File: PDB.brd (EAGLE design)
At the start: 143.5 x 151.3 mm, 71 parts

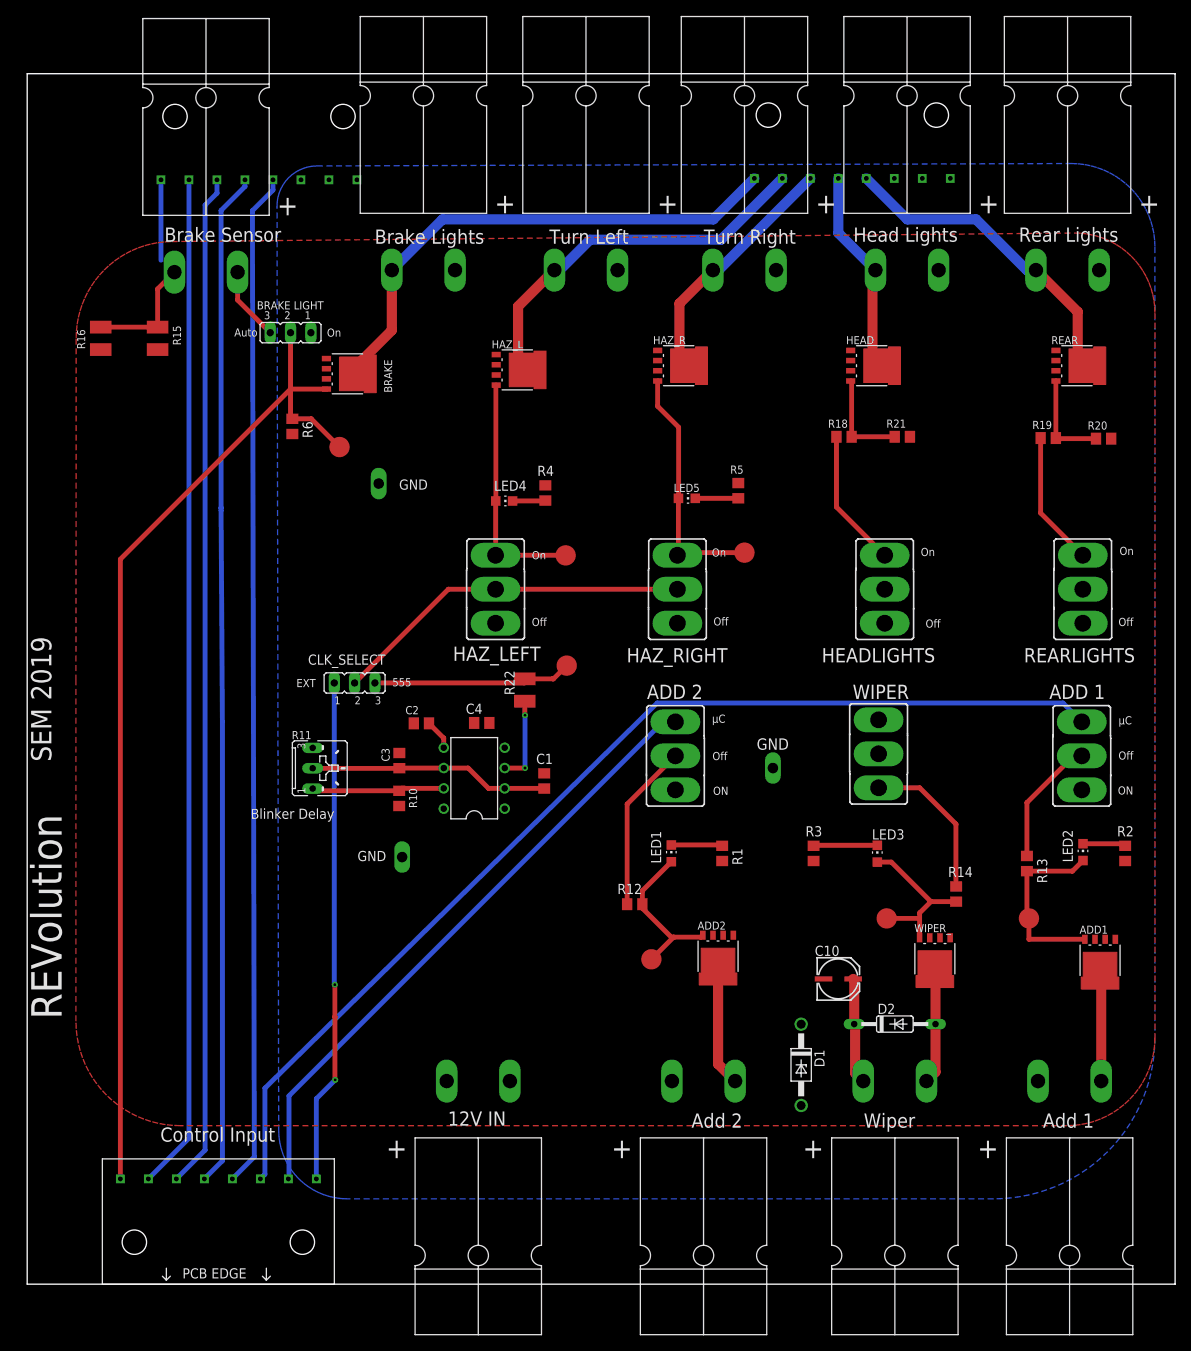
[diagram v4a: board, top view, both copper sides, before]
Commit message: added REV Logo, fixed some hidden airwires
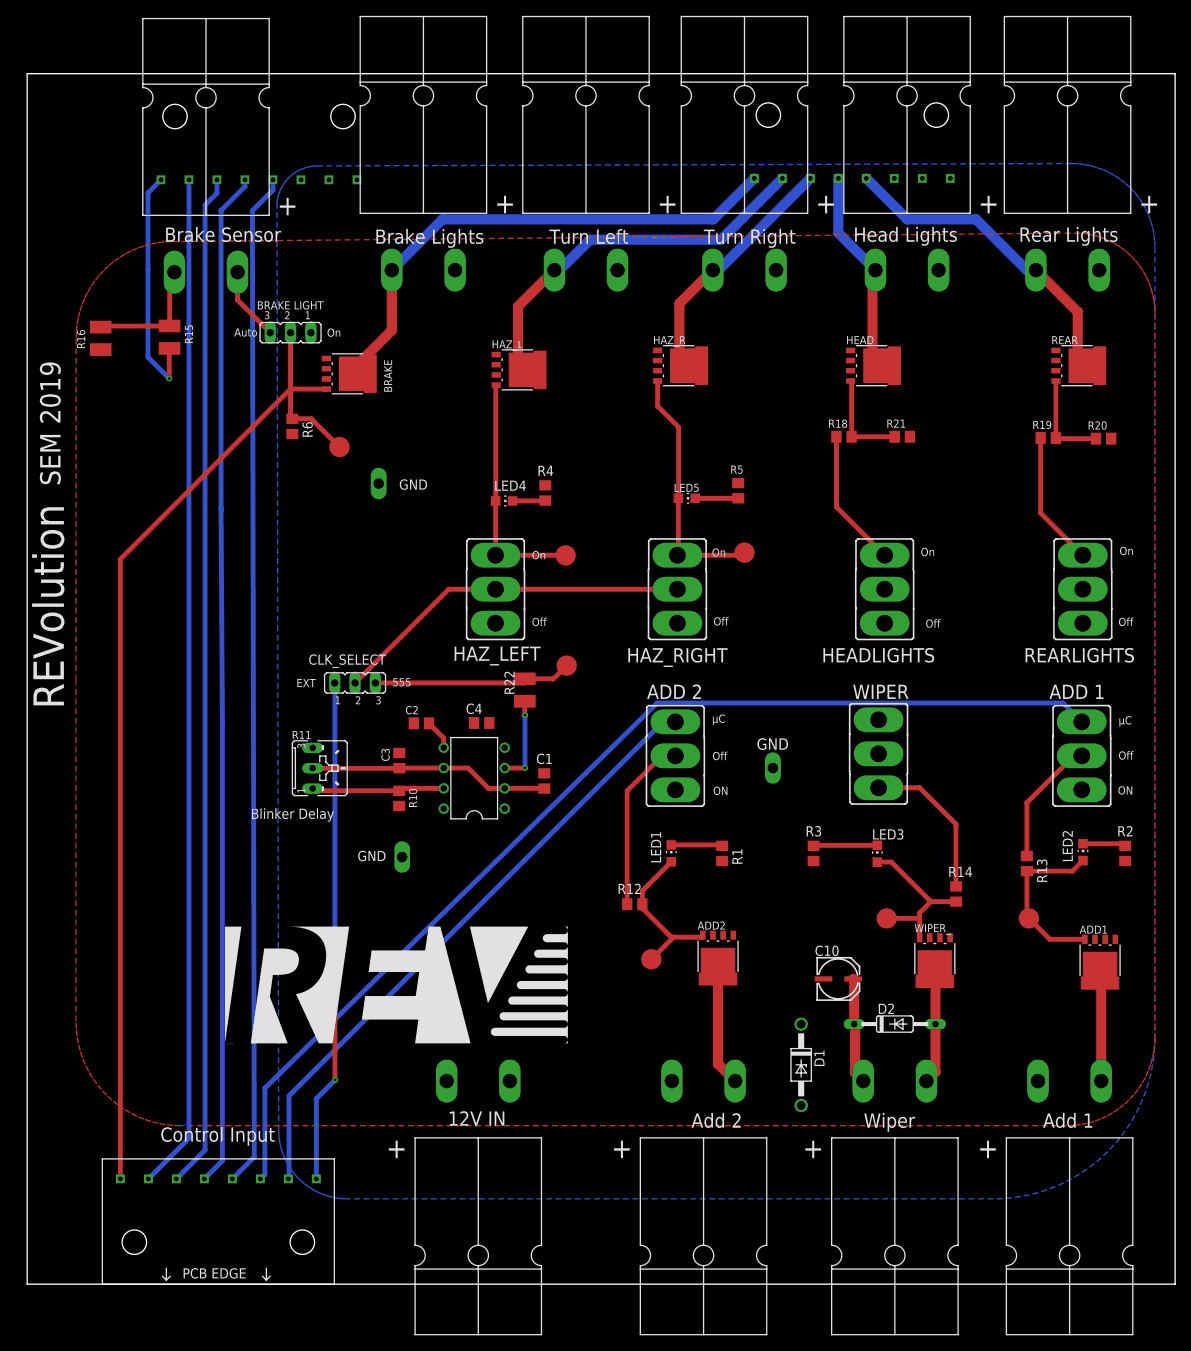
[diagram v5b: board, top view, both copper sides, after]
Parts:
- moved R15 1.51 mm to (26.2, 95.0)
- moved CLK_SELECT 0.06 mm to (49.4, 51.8)
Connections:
- new net BRAKE_SNS_OUT: BRAKE.4, BRAKE_SENSOR_OVERRIDE.2, CONTROL_IN.P1, R6.1, TP7.TP
- net BRAKE_SNS_IN: no longer BRAKE.4, BRAKE_SENSOR_OVERRIDE.2, CONTROL_IN.P1, R6.1, TP7.TP
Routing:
- net BRAKE_SNS_OUT: track 0.00 -> 130.2 mm
- net BRAKE_SNS_IN: track 139.5 -> 9.25 mm
- net VDD: track 23.4 -> 43.7 mm, vias 0 -> 1
- net N$26: track 23.2 -> 21.6 mm
- net H6: track 21.0 -> 22.0 mm
- net SNS_VOLTAGE: track 14.9 -> 15.7 mm
- net H2: track 30.8 -> 31.4 mm
- net H5: track 16.5 -> 15.9 mm
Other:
- board text added: "/Users/louissmidt/Downloads/Untitled-2.BMP"
- board text added: "SPI OUT"
- board text removed: "SPI PT OUT"

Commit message: fixes vdd plane, fixes issues discussed in meeting
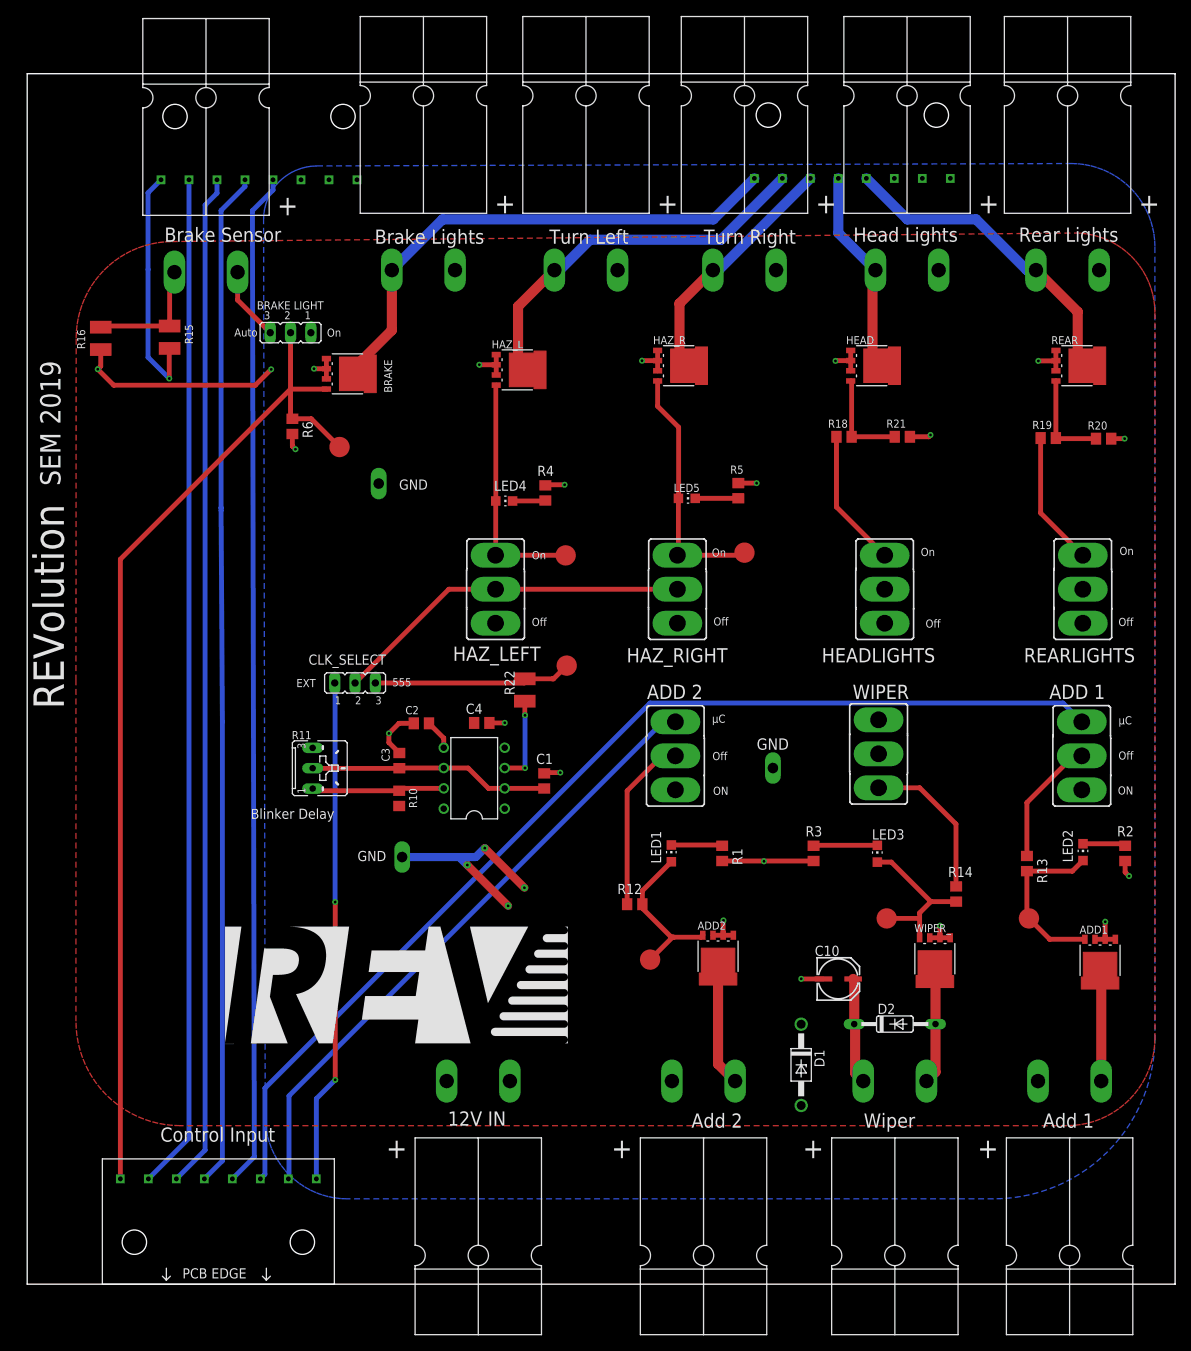
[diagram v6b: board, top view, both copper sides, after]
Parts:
- moved TP2 0.16 mm to (86.2, 17.2)
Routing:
- net GND: track 0.00 -> 126.1 mm, vias 0 -> 25
- net N$7: track 21.1 -> 20.4 mm
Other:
- board text added: "Standoffs"

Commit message: added values
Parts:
- D1: value (none) -> 12V
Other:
- board text removed: "Standoffs"
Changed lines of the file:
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@@
 <layer number="43" name="vRestrict" color="2" fill="10" visible="no" active="yes"/>
 <layer number="44" name="Drills" color="7" fill="1" visible="no" active="yes"/>
-<layer number="45" name="Holes" color="7" fill="1" visible="no" active="yes"/>
+<layer number="45" name="Holes" color="7" fill="1" visible="yes" active="yes"/>
 <layer number="46" name="Milling" color="3" fill="1" visible="no" active="yes"/>
 <layer number="47" name="Measures" color="7" fill="1" visible="no" active="yes"/>
@@
 <text x="36.322" y="34.798" size="1.27" layer="25">Blinker Delay</text>
 <text x="12.547" y="76.421" size="2.54" layer="25" font="vector" ratio="13" rot="R90">SEM 2019</text>
-<text x="12.97" y="48.522" size="3.81" layer="25" rot="R90">REVolution</text>
+<text x="12.97" y="29.222" size="3.81" layer="25" rot="R90">REVolution</text>
 <text x="92.964" y="106.68" size="1.778" layer="25">Turn Right</text>
 <text x="73.66" y="106.68" size="1.778" layer="25">Turn Left</text>
@@
 <rectangle x1="75.59" y1="21.31" x2="75.97" y2="21.33" layer="25"/>
 <text x="33.12" y="6.64" size="0.04" layer="25" font="vector">/Users/louissmidt/Downloads/Untitled-2.BMP</text>
-<text x="9.36" y="120.5" size="1.778" layer="26">Standoffs</text>
+<hole x="14.68" y="122.6" drill="2"/>
+<hole x="12.84" y="-18.42" drill="2"/>
+<hole x="149.16" y="121.88" drill="2"/>
+<hole x="148.68" y="-17.46" drill="2"/>
 </plain>
 <attributes>
@@
 <attribute name="VALUE" value="22uF" x="108.458" y="12.446" size="1.27" layer="27"/>
 </element>
-<element name="D1" library="diode" library_urn="urn:adsk.eagle:library:210" package="DO41Z10" package3d_urn="urn:adsk.eagle:package:43341/1" value="" x="105.129" y="4.048" smashed="yes" rot="R270">
+<element name="D1" library="diode" library_urn="urn:adsk.eagle:library:210" package="DO41Z10" package3d_urn="urn:adsk.eagle:package:43341/1" value="12V" x="105.129" y="4.048" smashed="yes" rot="R270">
 <attribute name="NAME" x="106.78" y="5.953" size="1.27" layer="25" ratio="10" rot="R270"/>
 <attribute name="VALUE" x="102.716" y="5.572" size="1.27" layer="27" ratio="10" rot="R270"/>
@@
 <contactref element="R6" pad="2"/>
 <contactref element="D1" pad="A"/>
-<contactref element="C1" pad="2"/>
 <contactref element="R21" pad="1"/>
 <contactref element="R20" pad="1"/>
-<contactref element="C2" pad="2"/>
-<contactref element="C3" pad="2"/>
 <contactref element="555" pad="1"/>
-<contactref element="C4" pad="2"/>
 <polygon width="0.1524" layer="16" isolate="0.254">
 <vertex x="129.192" y="-12.7"/>
@@
 <via x="100.48" y="29.5" extent="1-16" drill="0.35"/>
 <wire x1="106.68" y1="29.53" x2="100.45" y2="29.53" width="0.6096" layer="1"/>
-<wire x1="54.903" y1="43.027" x2="53.6" y2="44.33" width="0.6096" layer="1"/>
-<wire x1="53.6" y1="44.33" x2="53.6" y2="45.48" width="0.6096" layer="1"/>
-<via x="53.6" y="45.48" extent="1-16" drill="0.35"/>
-<wire x1="56.708" y1="46.736" x2="54.856" y2="46.736" width="0.6096" layer="1"/>
-<wire x1="54.856" y1="46.736" x2="53.6" y2="45.48" width="0.6096" layer="1"/>
-<wire x1="66.153" y1="46.786" x2="68.066" y2="46.786" width="0.6096" layer="1"/>
-<wire x1="68.066" y1="46.786" x2="68.08" y2="46.8" width="0.6096" layer="1"/>
-<via x="68.08" y="46.8" extent="1-16" drill="0.35"/>
-<wire x1="73.012" y1="40.487" x2="73.105" y2="40.58" width="0.6096" layer="1"/>
-<wire x1="73.105" y1="40.58" x2="75.02" y2="40.58" width="0.6096" layer="1"/>
-<via x="75.02" y="40.58" extent="1-16" drill="0.35"/>
 <wire x1="107.928" y1="14.786" x2="105.154" y2="14.786" width="0.6096" layer="1"/>
 <wire x1="105.154" y1="14.786" x2="105.14" y2="14.8" width="0.6096" layer="1"/>
@@
 <wire x1="65.58" y1="31.14" x2="70.54" y2="26.18" width="1.016" layer="1"/>
 <via x="70.54" y="26.18" extent="1-16" drill="0.35" diameter="0.9"/>
+<contactref element="C1" pad="2"/>
+<contactref element="C4" pad="2"/>
+<contactref element="C3" pad="2"/>
+<contactref element="C2" pad="2"/>
+<wire x1="66.153" y1="46.786" x2="68.066" y2="46.786" width="0.6096" layer="1"/>
+<wire x1="68.066" y1="46.786" x2="68.08" y2="46.8" width="0.6096" layer="1"/>
+<via x="68.08" y="46.8" extent="1-16" drill="0.35"/>
+<wire x1="73.012" y1="40.487" x2="73.105" y2="40.58" width="0.6096" layer="1"/>
+<wire x1="73.105" y1="40.58" x2="75.02" y2="40.58" width="0.6096" layer="1"/>
+<via x="75.02" y="40.58" extent="1-16" drill="0.35"/>
+<wire x1="54.903" y1="43.027" x2="53.6" y2="44.33" width="0.6096" layer="1"/>
+<wire x1="53.6" y1="44.33" x2="53.6" y2="45.48" width="0.6096" layer="1"/>
+<via x="53.6" y="45.48" extent="1-16" drill="0.35"/>
+<wire x1="53.6" y1="45.48" x2="54.856" y2="46.736" width="0.6096" layer="1"/>
+<wire x1="54.856" y1="46.736" x2="56.708" y2="46.736" width="0.6096" layer="1"/>
 </signal>
 <signal name="VDD">
